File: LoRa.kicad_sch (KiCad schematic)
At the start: 18 parts, among them J10 Conn_Coaxial, J6 Conn_Coaxial, U1 NCV8170AXV300T2G, U2 Quectel_L96, U5 E22-900M22S

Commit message: PCB component placement according to AIoT2
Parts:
- J10, J6: now not fitted
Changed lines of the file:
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@@
 		(on_board yes)
 		(in_pos_files yes)
-		(dnp no)
+		(dnp yes)
 		(fields_autoplaced yes)
 		(property "Reference" "J6"
@@
 		(on_board yes)
 		(in_pos_files yes)
-		(dnp no)
+		(dnp yes)
 		(fields_autoplaced yes)
 		(property "Reference" "J10"

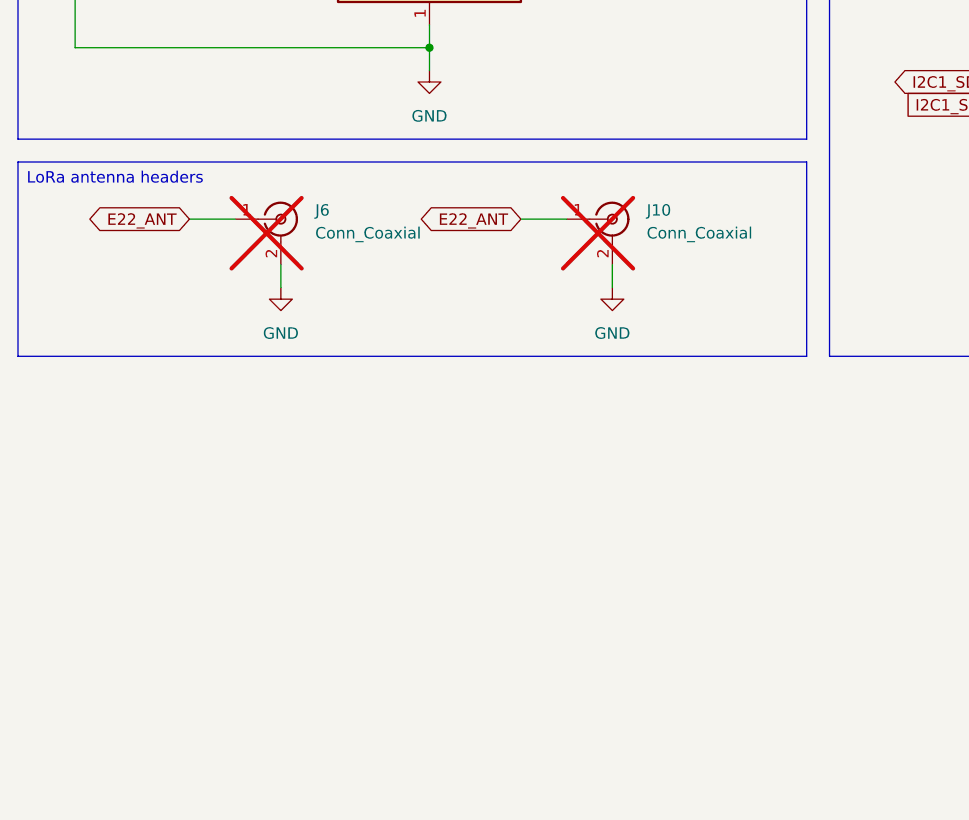
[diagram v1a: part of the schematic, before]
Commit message: pcb: pins for antenna, silkscreen…
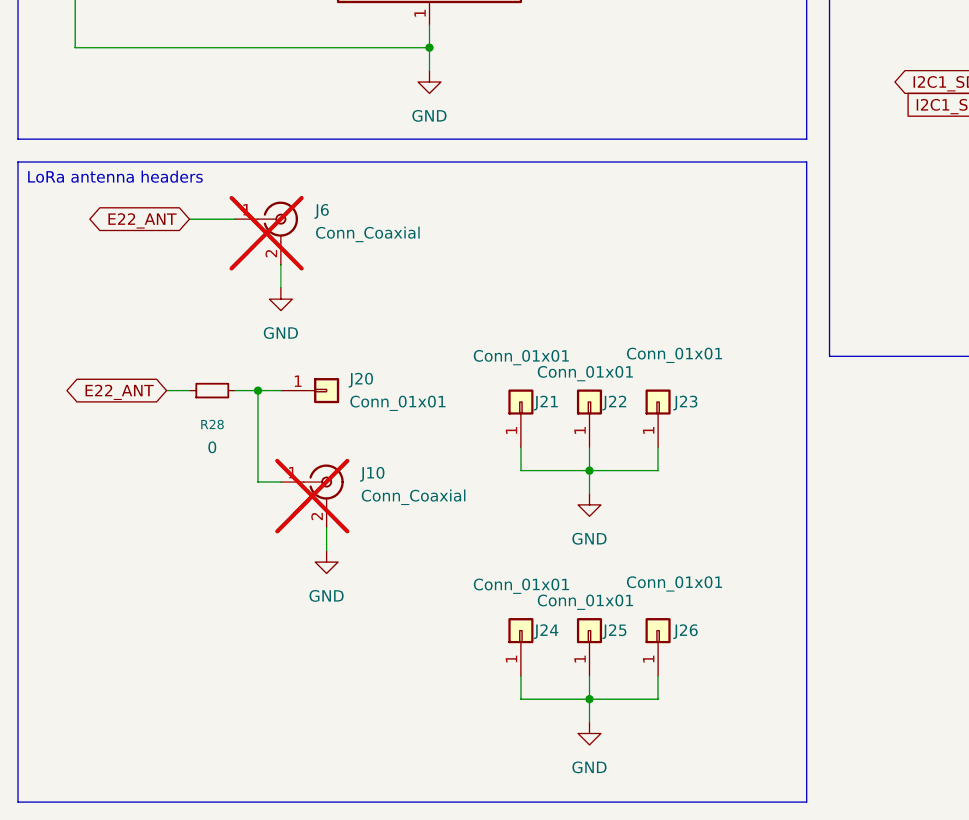
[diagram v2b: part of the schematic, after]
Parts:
- added J20, J21, J22, J23, J24, J25, J26: Conn_01x01, Connector_Pin:Pin_D1.0mm_L10.0mm, symbol Connector_Generic:Conn_01x01
- added R28: 0, Resistor_SMD:R_0805_2012Metric, symbol Device:R_Small
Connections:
- net E22_ANT: now also R28.1; no longer J10.1 (In)
- net GND: now also J21.1 (Pin_1), J22.1 (Pin_1), J23.1 (Pin_1), J24.1 (Pin_1), J25.1 (Pin_1), J26.1 (Pin_1)
- new net: J10.1 (In), J20.1 (Pin_1), R28.2
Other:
- moved on the sheet: J10
